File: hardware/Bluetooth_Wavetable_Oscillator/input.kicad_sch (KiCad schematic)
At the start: 28 parts, among them J3 AudioJack2_SwitchT, J4 AudioJack2_SwitchT, U4 TL074, U5 TL072

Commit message: add audio test files
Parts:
- C10, C11, C12, C9: footprint (none) -> Capacitor_THT:C_Disc_D5.0mm_W2.5mm_P5.00mm
- R10, R11, R12, R13, R14, R15, R16, R17, R18, R19, R6, R7, R8, R9: footprint (none) -> Resistor_THT:R_Axial_DIN0204_L3.6mm_D1.6mm_P7.62mm_Horizontal
- RV2, RV3: footprint (none) -> Potentiometer_THT:Potentiometer_Bourns_PTV09A-1_Single_Vertical
- U4: footprint (none) -> Package_DIP:DIP-14_W7.62mm
- U5: footprint (none) -> Package_DIP:DIP-8_W7.62mm
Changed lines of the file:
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@@
 			)
 		)
-		(property "Footprint" ""
+		(property "Footprint" "Resistor_THT:R_Axial_DIN0204_L3.6mm_D1.6mm_P7.62mm_Horizontal"
 			(at 138.43 139.192 90)
 			(effects
@@
 			)
 		)
-		(property "Footprint" ""
+		(property "Footprint" "Resistor_THT:R_Axial_DIN0204_L3.6mm_D1.6mm_P7.62mm_Horizontal"
 			(at 139.7 76.962 90)
 			(effects
@@
 			)
 		)
-		(property "Footprint" ""
+		(property "Footprint" "Resistor_THT:R_Axial_DIN0204_L3.6mm_D1.6mm_P7.62mm_Horizontal"
 			(at 160.02 66.802 90)
 			(effects
@@
 			)
 		)
-		(property "Footprint" ""
+		(property "Footprint" "Capacitor_THT:C_Disc_D5.0mm_W2.5mm_P5.00mm"
 			(at 39.0652 182.88 0)
 			(effects
@@
 			)
 		)
-		(property "Footprint" ""
+		(property "Footprint" "Resistor_THT:R_Axial_DIN0204_L3.6mm_D1.6mm_P7.62mm_Horizontal"
 			(at 119.38 135.128 90)
 			(effects
@@
 			)
 		)
-		(property "Footprint" ""
+		(property "Footprint" "Resistor_THT:R_Axial_DIN0204_L3.6mm_D1.6mm_P7.62mm_Horizontal"
 			(at 157.48 129.032 90)
 			(effects
@@
 			)
 		)
-		(property "Footprint" ""
+		(property "Footprint" "Potentiometer_THT:Potentiometer_Bourns_PTV09A-1_Single_Vertical"
 			(at 78.74 44.45 0)
 			(effects
@@
 			)
 		)
-		(property "Footprint" ""
+		(property "Footprint" "Resistor_THT:R_Axial_DIN0204_L3.6mm_D1.6mm_P7.62mm_Horizontal"
 			(at 194.31 130.048 90)
 			(effects
@@
 			)
 		)
-		(property "Footprint" ""
+		(property "Footprint" "Capacitor_THT:C_Disc_D5.0mm_W2.5mm_P5.00mm"
 			(at 127.9652 182.88 0)
 			(effects
@@
 			)
 		)
-		(property "Footprint" ""
+		(property "Footprint" "Resistor_THT:R_Axial_DIN0204_L3.6mm_D1.6mm_P7.62mm_Horizontal"
 			(at 177.8 77.978 90)
 			(effects
@@
 			)
 		)
-		(property "Footprint" ""
+		(property "Footprint" "Package_DIP:DIP-14_W7.62mm"
 			(at 175.26 125.73 0)
 			(effects
@@
 			)
 		)
-		(property "Footprint" ""
+		(property "Footprint" "Resistor_THT:R_Axial_DIN0204_L3.6mm_D1.6mm_P7.62mm_Horizontal"
 			(at 121.92 72.898 90)
 			(effects
@@
 			)
 		)
-		(property "Footprint" ""
+		(property "Footprint" "Resistor_THT:R_Axial_DIN0204_L3.6mm_D1.6mm_P7.62mm_Horizontal"
 			(at 85.852 125.73 90)
 			(effects
@@
 			)
 		)
-		(property "Footprint" ""
+		(property "Footprint" "Package_DIP:DIP-8_W7.62mm"
 			(at 100.33 46.99 0)
 			(effects
@@
 			)
 		)
-		(property "Footprint" ""
+		(property "Footprint" "Resistor_THT:R_Axial_DIN0204_L3.6mm_D1.6mm_P7.62mm_Horizontal"
 			(at 196.85 67.818 90)
 			(effects
@@
 			)
 		)
-		(property "Footprint" ""
+		(property "Footprint" "Package_DIP:DIP-14_W7.62mm"
 			(at 45.72 171.45 0)
 			(effects
@@
 			)
 		)
-		(property "Footprint" ""
+		(property "Footprint" "Resistor_THT:R_Axial_DIN0204_L3.6mm_D1.6mm_P7.62mm_Horizontal"
 			(at 175.26 140.208 90)
 			(effects
@@
 			)
 		)
-		(property "Footprint" ""
+		(property "Footprint" "Resistor_THT:R_Axial_DIN0204_L3.6mm_D1.6mm_P7.62mm_Horizontal"
 			(at 97.79 121.158 90)
 			(effects
@@
 			)
 		)
-		(property "Footprint" ""
+		(property "Footprint" "Resistor_THT:R_Axial_DIN0204_L3.6mm_D1.6mm_P7.62mm_Horizontal"
 			(at 89.662 63.5 90)
 			(effects
@@
 			)
 		)
-		(property "Footprint" ""
+		(property "Footprint" "Package_DIP:DIP-14_W7.62mm"
 			(at 176.53 63.5 0)
 			(effects
@@
 			)
 		)
-		(property "Footprint" ""
+		(property "Footprint" "Package_DIP:DIP-8_W7.62mm"
 			(at 116.84 170.18 0)
 			(effects
@@
 			)
 		)
-		(property "Footprint" ""
+		(property "Footprint" "Capacitor_THT:C_Disc_D5.0mm_W2.5mm_P5.00mm"
 			(at 107.6452 182.88 0)
 			(effects
@@
 			)
 		)
-		(property "Footprint" ""
+		(property "Footprint" "Package_DIP:DIP-14_W7.62mm"
 			(at 138.43 128.27 0)
 			(effects
@@
 			)
 		)
-		(property "Footprint" ""
+		(property "Footprint" "Package_DIP:DIP-14_W7.62mm"
 			(at 139.7 66.04 0)
 			(effects
@@
 			)
 		)
-		(property "Footprint" ""
+		(property "Footprint" "Capacitor_THT:C_Disc_D5.0mm_W2.5mm_P5.00mm"
 			(at 59.3852 182.88 0)
 			(effects
@@
 			)
 		)
-		(property "Footprint" ""
+		(property "Footprint" "Package_DIP:DIP-8_W7.62mm"
 			(at 96.52 109.22 0)
 			(effects
@@
 			)
 		)
-		(property "Footprint" ""
+		(property "Footprint" "Potentiometer_THT:Potentiometer_Bourns_PTV09A-1_Single_Vertical"
 			(at 74.93 106.68 0)
 			(effects
@@
 			)
 		)
-		(property "Footprint" ""
+		(property "Footprint" "Resistor_THT:R_Axial_DIN0204_L3.6mm_D1.6mm_P7.62mm_Horizontal"
 			(at 101.6 58.928 90)
 			(effects

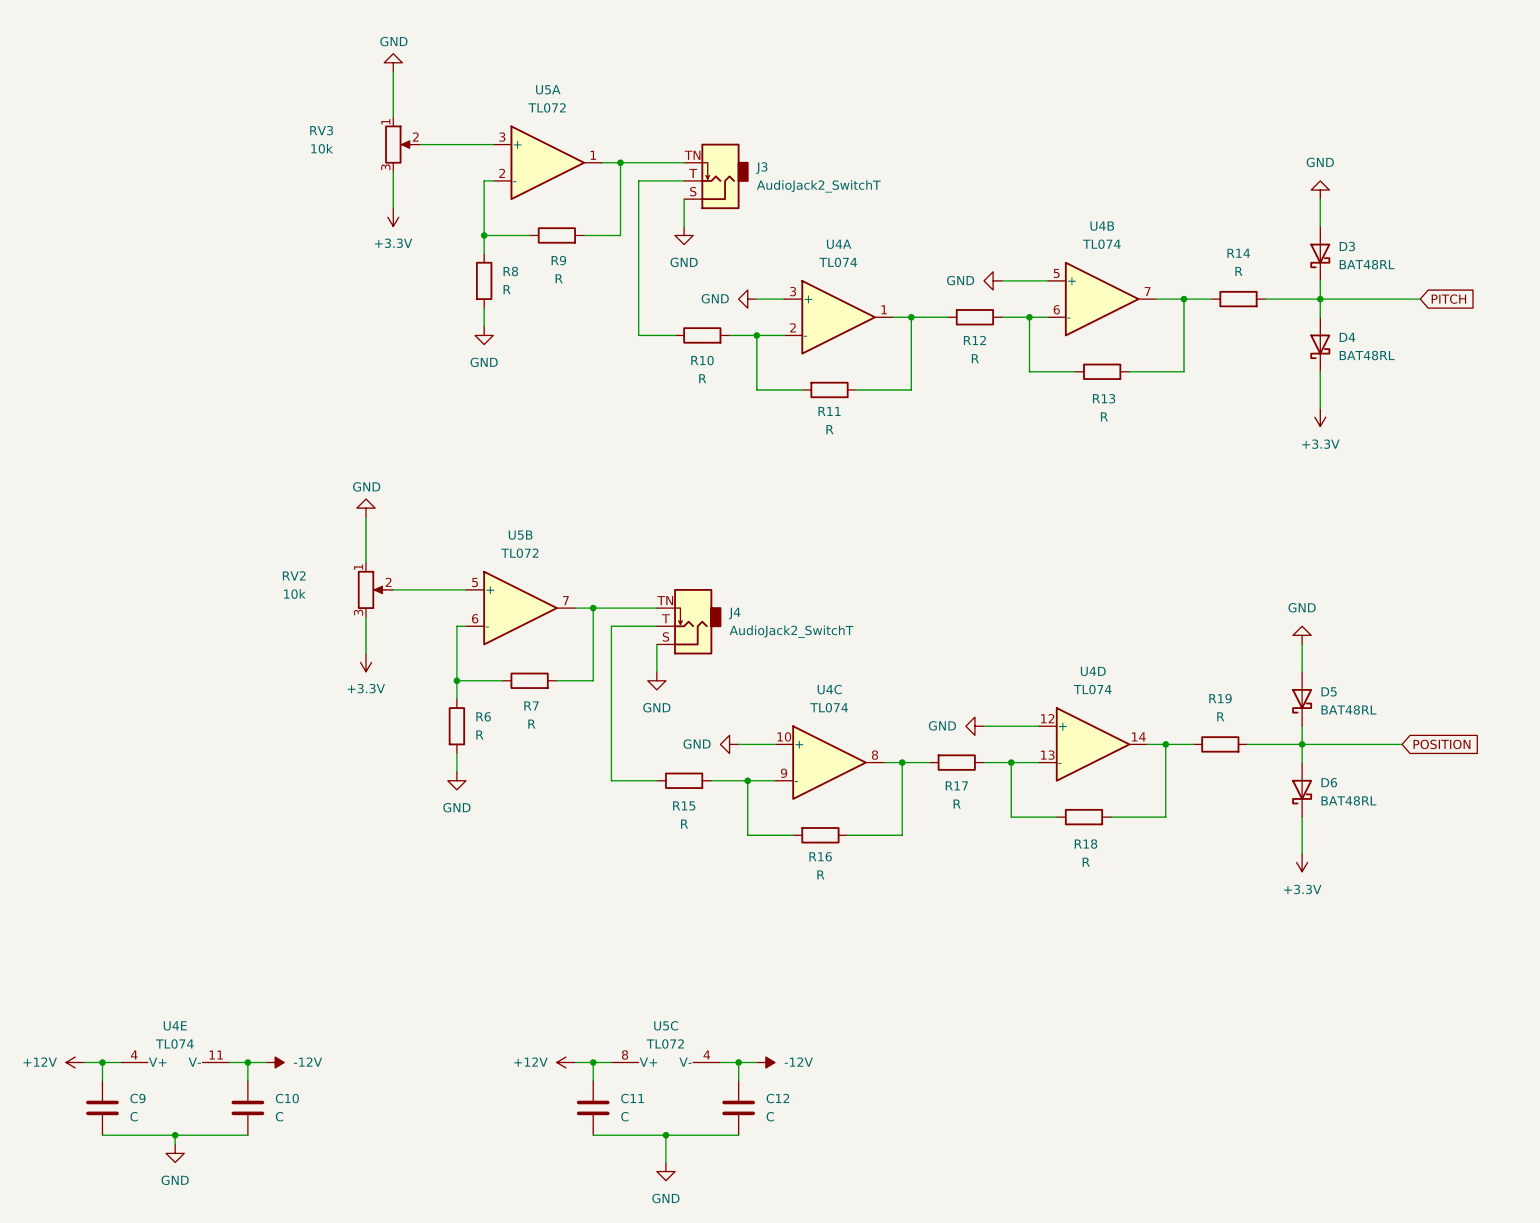
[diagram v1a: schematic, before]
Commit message: add bth components, add component values, update SPI pins, change disp power supply to 5V
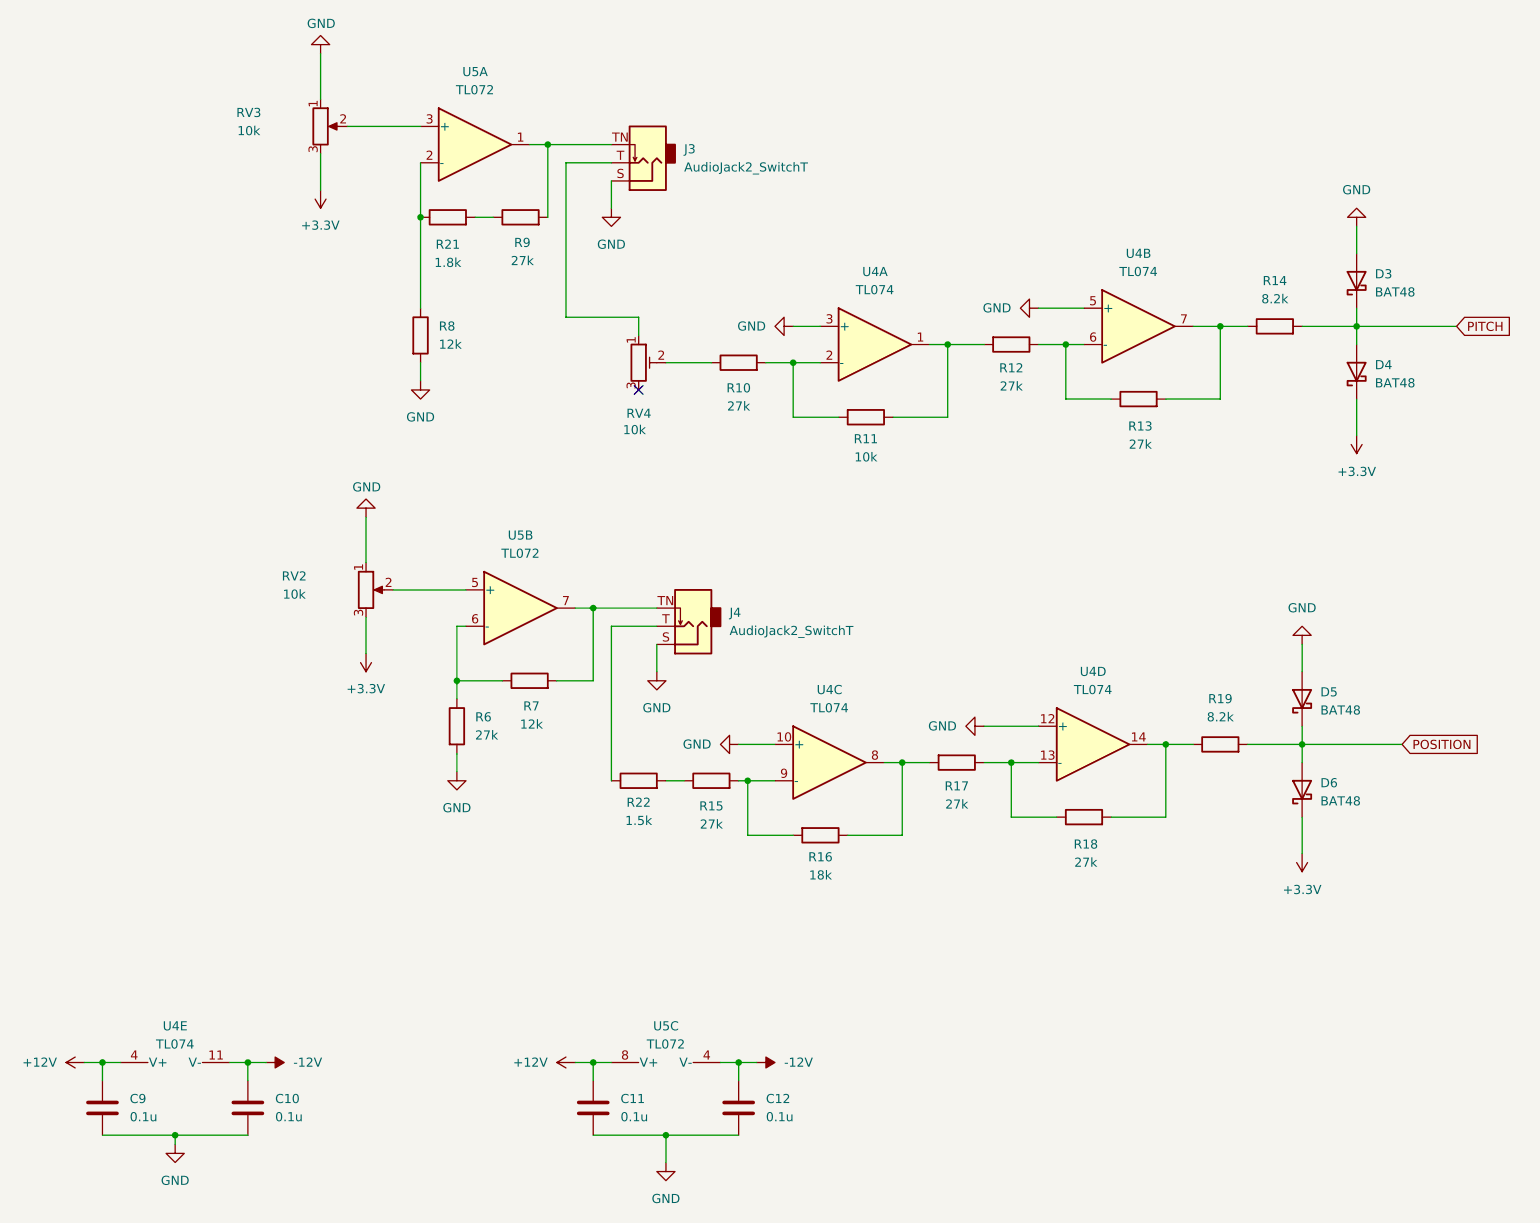
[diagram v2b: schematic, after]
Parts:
- added R21: 1.8k, symbol Device:R
- added R22: 1.5k, symbol Device:R
- added RV4: 10k, symbol Device:R_Potentiometer_Trim
- C10, C11, C12, C9: value C -> 0.1u
- D3, D4, D5, D6: value BAT48RL -> BAT48
- R10, R12, R13, R15, R17, R18, R6, R9: value R -> 27k
- R11: value R -> 10k
- R14, R19: value R -> 8.2k
- R16: value R -> 18k
- R7, R8: value R -> 12k
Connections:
- net at R15.1: now also R22.2; no longer J4.T
- net at J3.T: now also RV4.1; no longer R10.1
- net at R8.1, U5.2 (-): now also R21.1; no longer R9.1
- new net: R21.2, R9.1
- new net: R10.1, RV4.2
- new net: J4.T, R22.1
- no-connect marks 0 -> 1
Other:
- moved on the sheet: D3, D4, J3, R10, R11, R12, R13, R14, R15, R8, R9, RV3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

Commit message: start PCB layout
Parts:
- J3, J4: footprint (none) -> Connector_Audio:Jack_3.5mm_QingPu_WQP-PJ398SM_Vertical_CircularHoles
- R10, R11, R12, R13, R15, R16, R17, R18, R6, R7, R8, R9: footprint Resistor_THT:R_Axial_DIN0204_L3.6mm_D1.6mm_P7.62mm_Horizontal -> Resistor_THT:R_Axial_DIN0204_L3.6mm_D1.6mm_P2.54mm_Vertical
- R21, R22: footprint (none) -> Resistor_THT:R_Axial_DIN0204_L3.6mm_D1.6mm_P2.54mm_Vertical
- RV4: footprint (none) -> Trimmer-potentiometer:Trimmer-potentiometer
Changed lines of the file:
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@@
 			)
 		)
-		(property "Footprint" "Resistor_THT:R_Axial_DIN0204_L3.6mm_D1.6mm_P7.62mm_Horizontal"
+		(property "Footprint" "Resistor_THT:R_Axial_DIN0204_L3.6mm_D1.6mm_P2.54mm_Vertical"
 			(at 138.43 139.192 90)
 			(effects
@@
 			)
 		)
-		(property "Footprint" "Resistor_THT:R_Axial_DIN0204_L3.6mm_D1.6mm_P7.62mm_Horizontal"
+		(property "Footprint" "Resistor_THT:R_Axial_DIN0204_L3.6mm_D1.6mm_P2.54mm_Vertical"
 			(at 144.78 80.772 90)
 			(effects
@@
 			)
 		)
-		(property "Footprint" ""
+		(property "Footprint" "Resistor_THT:R_Axial_DIN0204_L3.6mm_D1.6mm_P2.54mm_Vertical"
 			(at 86.36 56.388 90)
 			(effects
@@
 			)
 		)
-		(property "Footprint" "Resistor_THT:R_Axial_DIN0204_L3.6mm_D1.6mm_P7.62mm_Horizontal"
+		(property "Footprint" "Resistor_THT:R_Axial_DIN0204_L3.6mm_D1.6mm_P2.54mm_Vertical"
 			(at 165.1 70.612 90)
 			(effects
@@
 			)
 		)
-		(property "Footprint" "Resistor_THT:R_Axial_DIN0204_L3.6mm_D1.6mm_P7.62mm_Horizontal"
+		(property "Footprint" "Resistor_THT:R_Axial_DIN0204_L3.6mm_D1.6mm_P2.54mm_Vertical"
 			(at 123.19 135.128 90)
 			(effects
@@
 			)
 		)
-		(property "Footprint" "Resistor_THT:R_Axial_DIN0204_L3.6mm_D1.6mm_P7.62mm_Horizontal"
+		(property "Footprint" "Resistor_THT:R_Axial_DIN0204_L3.6mm_D1.6mm_P2.54mm_Vertical"
 			(at 157.48 129.032 90)
 			(effects
@@
 			)
 		)
-		(property "Footprint" ""
+		(property "Footprint" "Trimmer-potentiometer:Trimmer-potentiometer"
 			(at 113.03 74.93 0)
 			(effects
@@
 			)
 		)
-		(property "Footprint" ""
+		(property "Footprint" "Connector_Audio:Jack_3.5mm_QingPu_WQP-PJ398SM_Vertical_CircularHoles"
 			(at 120.65 111.76 0)
 			(effects
@@
 			)
 		)
-		(property "Footprint" "Resistor_THT:R_Axial_DIN0204_L3.6mm_D1.6mm_P7.62mm_Horizontal"
+		(property "Footprint" "Resistor_THT:R_Axial_DIN0204_L3.6mm_D1.6mm_P2.54mm_Vertical"
 			(at 182.88 81.788 90)
 			(effects
@@
 			)
 		)
-		(property "Footprint" "Resistor_THT:R_Axial_DIN0204_L3.6mm_D1.6mm_P7.62mm_Horizontal"
+		(property "Footprint" "Resistor_THT:R_Axial_DIN0204_L3.6mm_D1.6mm_P2.54mm_Vertical"
 			(at 127 76.708 90)
 			(effects
@@
 			)
 		)
-		(property "Footprint" "Resistor_THT:R_Axial_DIN0204_L3.6mm_D1.6mm_P7.62mm_Horizontal"
+		(property "Footprint" "Resistor_THT:R_Axial_DIN0204_L3.6mm_D1.6mm_P2.54mm_Vertical"
 			(at 85.852 125.73 90)
 			(effects
@@
 			)
 		)
-		(property "Footprint" "Resistor_THT:R_Axial_DIN0204_L3.6mm_D1.6mm_P7.62mm_Horizontal"
+		(property "Footprint" "Resistor_THT:R_Axial_DIN0204_L3.6mm_D1.6mm_P2.54mm_Vertical"
 			(at 175.26 140.208 90)
 			(effects
@@
 			)
 		)
-		(property "Footprint" "Resistor_THT:R_Axial_DIN0204_L3.6mm_D1.6mm_P7.62mm_Horizontal"
+		(property "Footprint" "Resistor_THT:R_Axial_DIN0204_L3.6mm_D1.6mm_P2.54mm_Vertical"
 			(at 97.79 121.158 90)
 			(effects
@@
 			)
 		)
-		(property "Footprint" "Resistor_THT:R_Axial_DIN0204_L3.6mm_D1.6mm_P7.62mm_Horizontal"
+		(property "Footprint" "Resistor_THT:R_Axial_DIN0204_L3.6mm_D1.6mm_P2.54mm_Vertical"
 			(at 80.772 71.12 90)
 			(effects
@@
 			)
 		)
-		(property "Footprint" ""
+		(property "Footprint" "Resistor_THT:R_Axial_DIN0204_L3.6mm_D1.6mm_P2.54mm_Vertical"
 			(at 113.03 135.128 90)
 			(effects
@@
 			)
 		)
-		(property "Footprint" ""
+		(property "Footprint" "Connector_Audio:Jack_3.5mm_QingPu_WQP-PJ398SM_Vertical_CircularHoles"
 			(at 114.3 46.99 0)
 			(effects
@@
 			)
 		)
-		(property "Footprint" "Resistor_THT:R_Axial_DIN0204_L3.6mm_D1.6mm_P7.62mm_Horizontal"
+		(property "Footprint" "Resistor_THT:R_Axial_DIN0204_L3.6mm_D1.6mm_P2.54mm_Vertical"
 			(at 96.52 56.388 90)
 			(effects

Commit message: update shematic, PCB and footprints
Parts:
- D3, D4, D5, D6: footprint Diode_THT:D_DO-35_SOD27_P7.62mm_Horizontal -> Diode_THT:D_DO-35_SOD27_P2.54mm_Vertical_KathodeUp
- R14, R19: footprint Resistor_THT:R_Axial_DIN0204_L3.6mm_D1.6mm_P7.62mm_Horizontal -> Resistor_THT:R_Axial_DIN0204_L3.6mm_D1.6mm_P2.54mm_Vertical
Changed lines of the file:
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@@
 			)
 		)
-		(property "Footprint" "Diode_THT:D_DO-35_SOD27_P7.62mm_Horizontal"
+		(property "Footprint" "Diode_THT:D_DO-35_SOD27_P2.54mm_Vertical_KathodeUp"
 			(at 210.185 134.62 0)
 			(effects
@@
 			)
 		)
-		(property "Footprint" "Diode_THT:D_DO-35_SOD27_P7.62mm_Horizontal"
+		(property "Footprint" "Diode_THT:D_DO-35_SOD27_P2.54mm_Vertical_KathodeUp"
 			(at 210.185 121.92 0)
 			(effects
@@
 			)
 		)
-		(property "Footprint" "Diode_THT:D_DO-35_SOD27_P7.62mm_Horizontal"
+		(property "Footprint" "Diode_THT:D_DO-35_SOD27_P2.54mm_Vertical_KathodeUp"
 			(at 217.805 76.2 0)
 			(effects
@@
 			)
 		)
-		(property "Footprint" "Resistor_THT:R_Axial_DIN0204_L3.6mm_D1.6mm_P7.62mm_Horizontal"
+		(property "Footprint" "Resistor_THT:R_Axial_DIN0204_L3.6mm_D1.6mm_P2.54mm_Vertical"
 			(at 194.31 130.048 90)
 			(effects
@@
 			)
 		)
-		(property "Footprint" "Resistor_THT:R_Axial_DIN0204_L3.6mm_D1.6mm_P7.62mm_Horizontal"
+		(property "Footprint" "Resistor_THT:R_Axial_DIN0204_L3.6mm_D1.6mm_P2.54mm_Vertical"
 			(at 201.93 71.628 90)
 			(effects
@@
 			)
 		)
-		(property "Footprint" "Diode_THT:D_DO-35_SOD27_P7.62mm_Horizontal"
+		(property "Footprint" "Diode_THT:D_DO-35_SOD27_P2.54mm_Vertical_KathodeUp"
 			(at 217.805 63.5 0)
 			(effects

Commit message: all items connected
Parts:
- D3, D4, D5, D6: footprint Diode_THT:D_DO-35_SOD27_P2.54mm_Vertical_KathodeUp -> Diode_THT:D_DO-34_SOD68_P7.62mm_Horizontal
- R6, R7: footprint Resistor_THT:R_Axial_DIN0204_L3.6mm_D1.6mm_P2.54mm_Vertical -> Resistor_THT:R_Axial_DIN0204_L3.6mm_D1.6mm_P7.62mm_Horizontal
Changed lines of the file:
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@@
 			)
 		)
-		(property "Footprint" "Diode_THT:D_DO-35_SOD27_P2.54mm_Vertical_KathodeUp"
+		(property "Footprint" "Diode_THT:D_DO-34_SOD68_P7.62mm_Horizontal"
 			(at 210.185 134.62 0)
 			(effects
@@
 			)
 		)
-		(property "Footprint" "Diode_THT:D_DO-35_SOD27_P2.54mm_Vertical_KathodeUp"
+		(property "Footprint" "Diode_THT:D_DO-34_SOD68_P7.62mm_Horizontal"
 			(at 210.185 121.92 0)
 			(effects
@@
 			)
 		)
-		(property "Footprint" "Diode_THT:D_DO-35_SOD27_P2.54mm_Vertical_KathodeUp"
+		(property "Footprint" "Diode_THT:D_DO-34_SOD68_P7.62mm_Horizontal"
 			(at 217.805 76.2 0)
 			(effects
@@
 			)
 		)
-		(property "Footprint" "Resistor_THT:R_Axial_DIN0204_L3.6mm_D1.6mm_P2.54mm_Vertical"
+		(property "Footprint" "Resistor_THT:R_Axial_DIN0204_L3.6mm_D1.6mm_P7.62mm_Horizontal"
 			(at 85.852 125.73 90)
 			(effects
@@
 			)
 		)
-		(property "Footprint" "Resistor_THT:R_Axial_DIN0204_L3.6mm_D1.6mm_P2.54mm_Vertical"
+		(property "Footprint" "Resistor_THT:R_Axial_DIN0204_L3.6mm_D1.6mm_P7.62mm_Horizontal"
 			(at 97.79 121.158 90)
 			(effects
@@
 			)
 		)
-		(property "Footprint" "Diode_THT:D_DO-35_SOD27_P2.54mm_Vertical_KathodeUp"
+		(property "Footprint" "Diode_THT:D_DO-34_SOD68_P7.62mm_Horizontal"
 			(at 217.805 63.5 0)
 			(effects
